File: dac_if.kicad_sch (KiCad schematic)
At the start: 0 parts

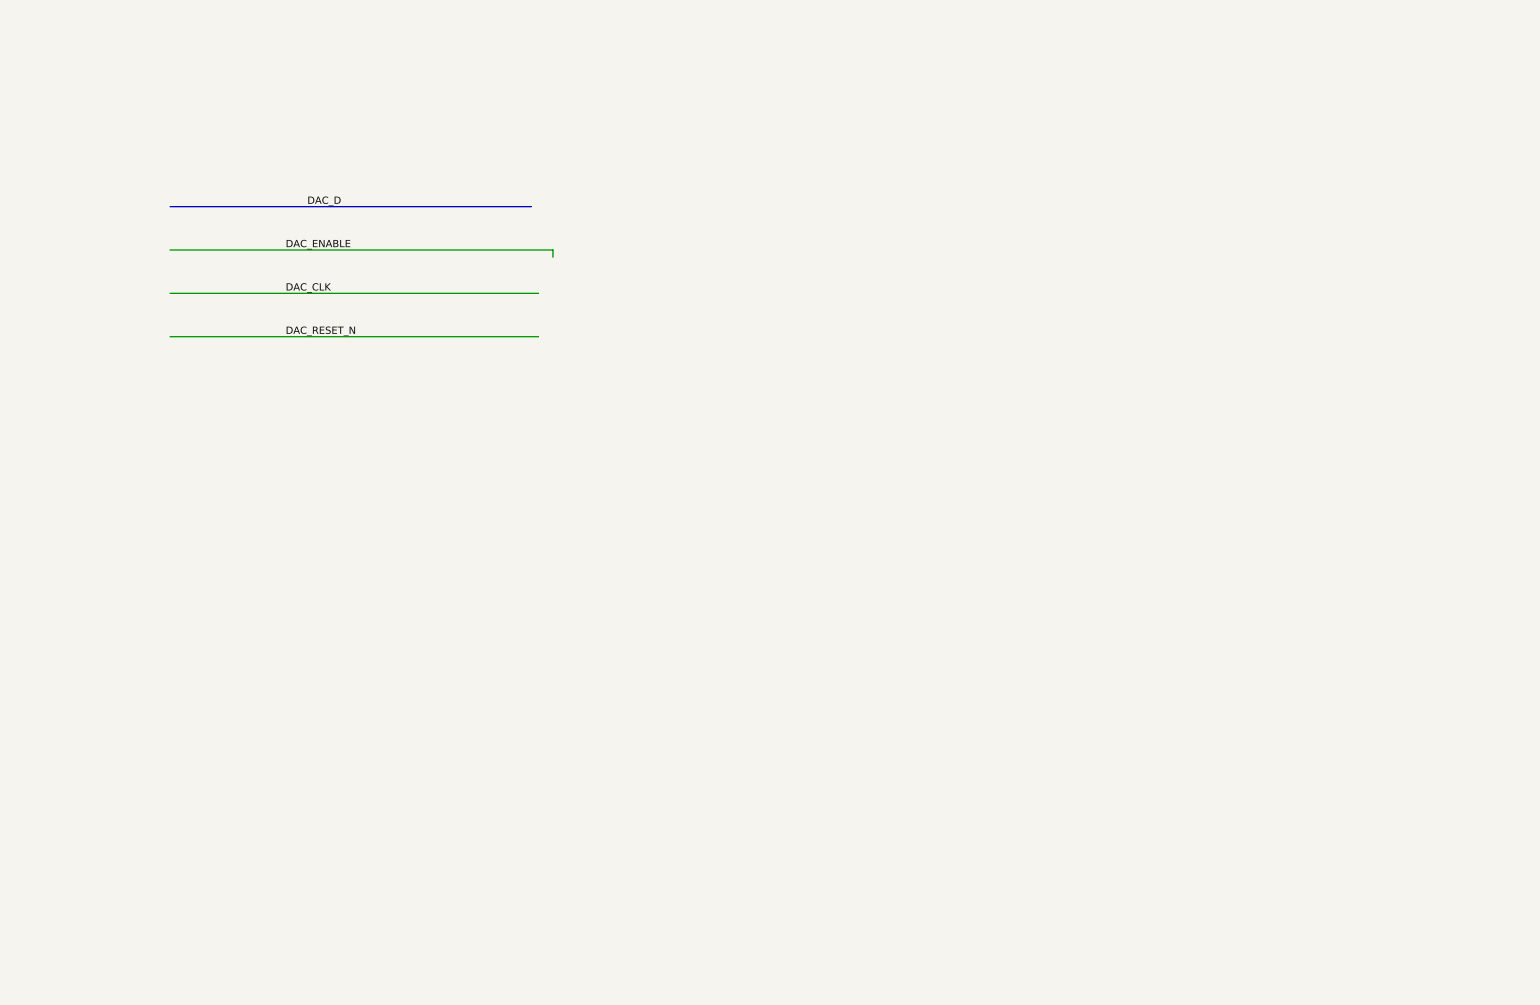
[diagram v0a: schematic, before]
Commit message: Turn to new version Kicad
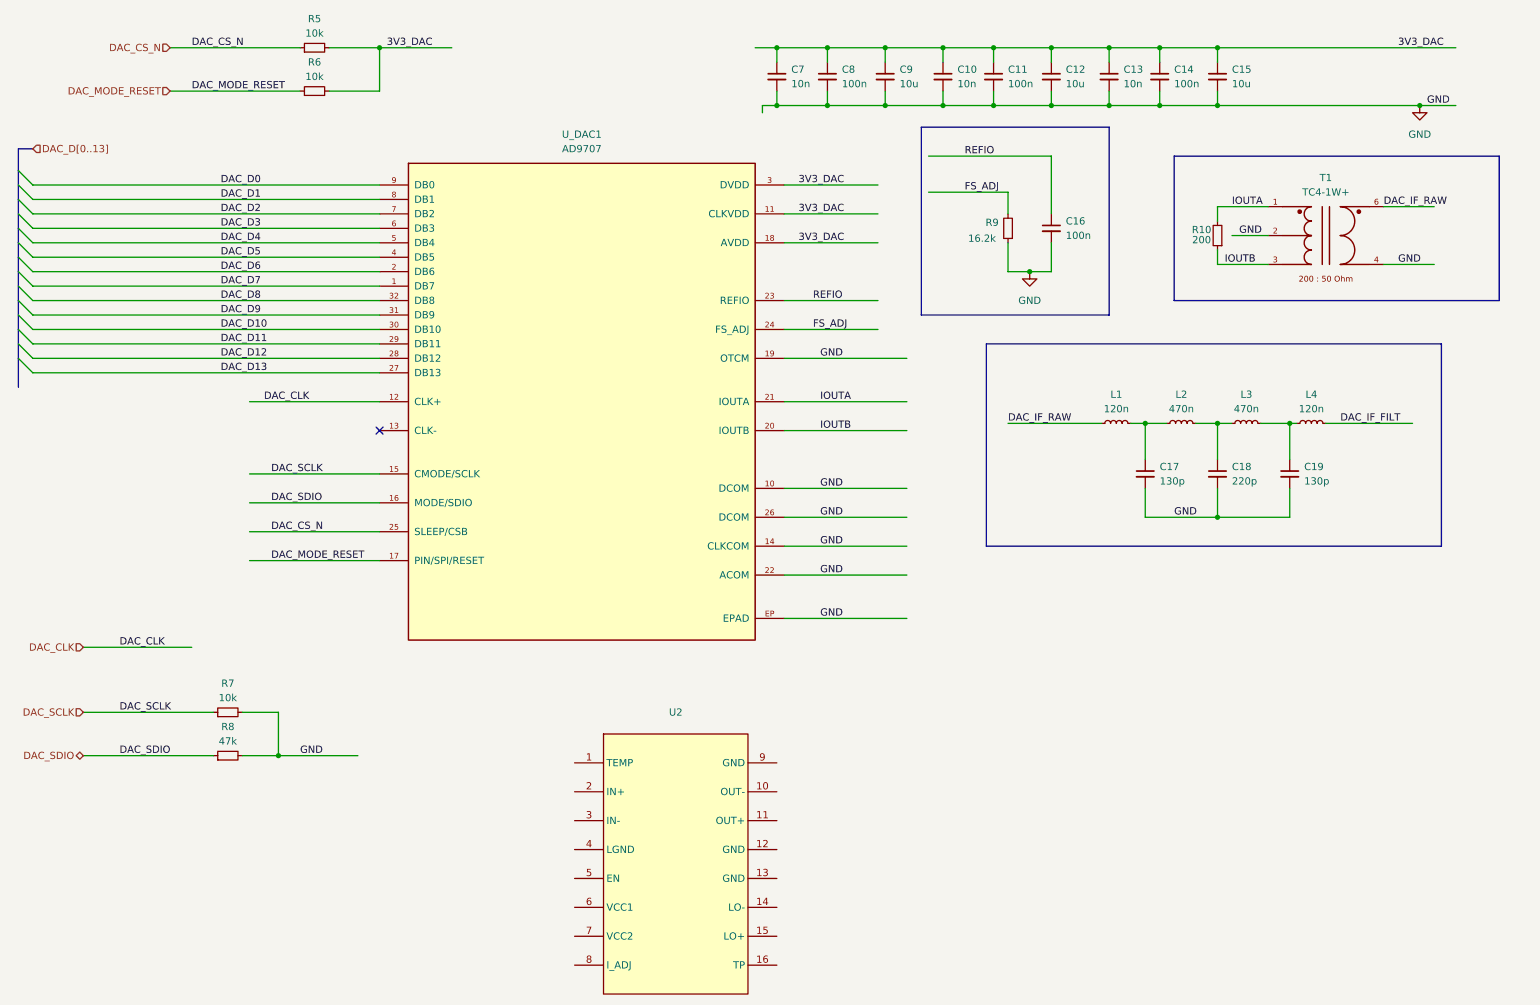
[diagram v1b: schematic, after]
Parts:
- added C10, C13, C7: 10n, Capacitor_SMD:C_0603_1608Metric, symbol Device:C_Small
- added C11, C14, C8: 100n, Capacitor_SMD:C_0603_1608Metric, symbol Device:C_Small
- added C12, C15, C9: 10u, Capacitor_SMD:C_1206_3216Metric, symbol Device:C_Small
- added C16: 100n, Capacitor_SMD:C_1206_3216Metric, symbol Device:C_Small
- added C17, C19: 130p, Capacitor_SMD:C_0603_1608Metric, symbol Device:C_Small
- added C18: 220p, Capacitor_SMD:C_0603_1608Metric, symbol Device:C_Small
- added L1, L4: 120n, Inductor_SMD:L_0603_1608Metric_Pad1.05x0.95mm_HandSolder, symbol Device:L_Small
- added L2, L3: 470n, Inductor_SMD:L_0603_1608Metric_Pad1.05x0.95mm_HandSolder, symbol Device:L_Small
- added R10: 200, Resistor_SMD:R_0603_1608Metric_Pad0.98x0.95mm_HandSolder, symbol Device:R_Small
- added R5, R6, R7: 10k, Resistor_SMD:R_0603_1608Metric_Pad0.98x0.95mm_HandSolder, symbol Device:R_Small
- added R8: 47k, Resistor_SMD:R_0603_1608Metric_Pad0.98x0.95mm_HandSolder, symbol Device:R_Small
- added R9: 16.2k, Resistor_SMD:R_0603_1608Metric_Pad0.98x0.95mm_HandSolder, symbol Device:R_Small
- added T1: TC4-1W+, GNSS_Transformers:TC4-1W_AT224-1A, symbol GNSS_Transformers:TC4-1W+
- added U2: (no value), Package_DFN_QFN:QFN-16-1EP_3x3mm_P0.5mm_EP1.7x1.7mm_ThermalVias, symbol gnss-lib:LTC5510
- added U_DAC1: AD9707, Package_CSP:LFCSP-32-1EP_5x5mm_P0.5mm_EP3.1x3.1mm, symbol GNSS_Draft:AD9707_RevF
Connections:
- net DAC_CLK: now also U_DAC1.12 (CLK+)
- new net: C18.1, L2.2, L3.1
- new net: C19.1, L3.2, L4.1
- new net: C17.1, L1.2, L2.1
- new net 3V3_DAC: C10.1, C11.1, C12.1, C13.1, C14.1, C15.1, C7.1, C8.1, C9.1, R5.2, R6.2, U_DAC1.11 (CLKVDD), U_DAC1.18 (AVDD), U_DAC1.3 (DVDD)
- new net DAC_CS_N: R5.1, U_DAC1.25 (SLEEP/CSB)
- new net DAC_D0: U_DAC1.9 (DB0)
- new net DAC_D1: U_DAC1.8 (DB1)
- new net DAC_D10: U_DAC1.30 (DB10)
- new net DAC_D11: U_DAC1.29 (DB11)
- new net DAC_D12: U_DAC1.28 (DB12)
- new net DAC_D13: U_DAC1.27 (DB13)
- new net DAC_D2: U_DAC1.7 (DB2)
- new net DAC_D3: U_DAC1.6 (DB3)
- new net DAC_D4: U_DAC1.5 (DB4)
- new net DAC_D5: U_DAC1.4 (DB5)
- new net DAC_D6: U_DAC1.2 (DB6)
- new net DAC_D7: U_DAC1.1 (DB7)
- new net DAC_D8: U_DAC1.32 (DB8)
- new net DAC_D9: U_DAC1.31 (DB9)
- new net DAC_IF_FILT: L4.2
- new net DAC_IF_RAW: L1.1, T1.6 (PRI_DOT)
- new net DAC_MODE_RESET: R6.1, U_DAC1.17 (PIN/SPI/RESET)
- new net DAC_SCLK: R7.1, U_DAC1.15 (CMODE/SCLK)
- new net DAC_SDIO: R8.1, U_DAC1.16 (MODE/SDIO)
- new net FS_ADJ: R9.2, U_DAC1.24 (FS_ADJ)
- new net GND: C10.2, C11.2, C12.2, C13.2, C14.2, C15.2, C16.2, C17.2, C18.2, C19.2, C7.2, C8.2, C9.2, R7.2, R8.2, R9.1, T1.2 (SEC_CT), T1.4 (PRI), U_DAC1.10 (DCOM), U_DAC1.14 (CLKCOM), U_DAC1.19 (OTCM), U_DAC1.22 (ACOM), U_DAC1.26 (DCOM), U_DAC1.EP (EPAD)
- new net IOUTA: R10.2, T1.1 (SEC_DOT), U_DAC1.21 (IOUTA)
- new net IOUTB: R10.1, T1.3 (SEC), U_DAC1.20 (IOUTB)
- new net REFIO: C16.1, U_DAC1.23 (REFIO)
- no-connect marks 0 -> 1

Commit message: Make schema of dac and rf partly
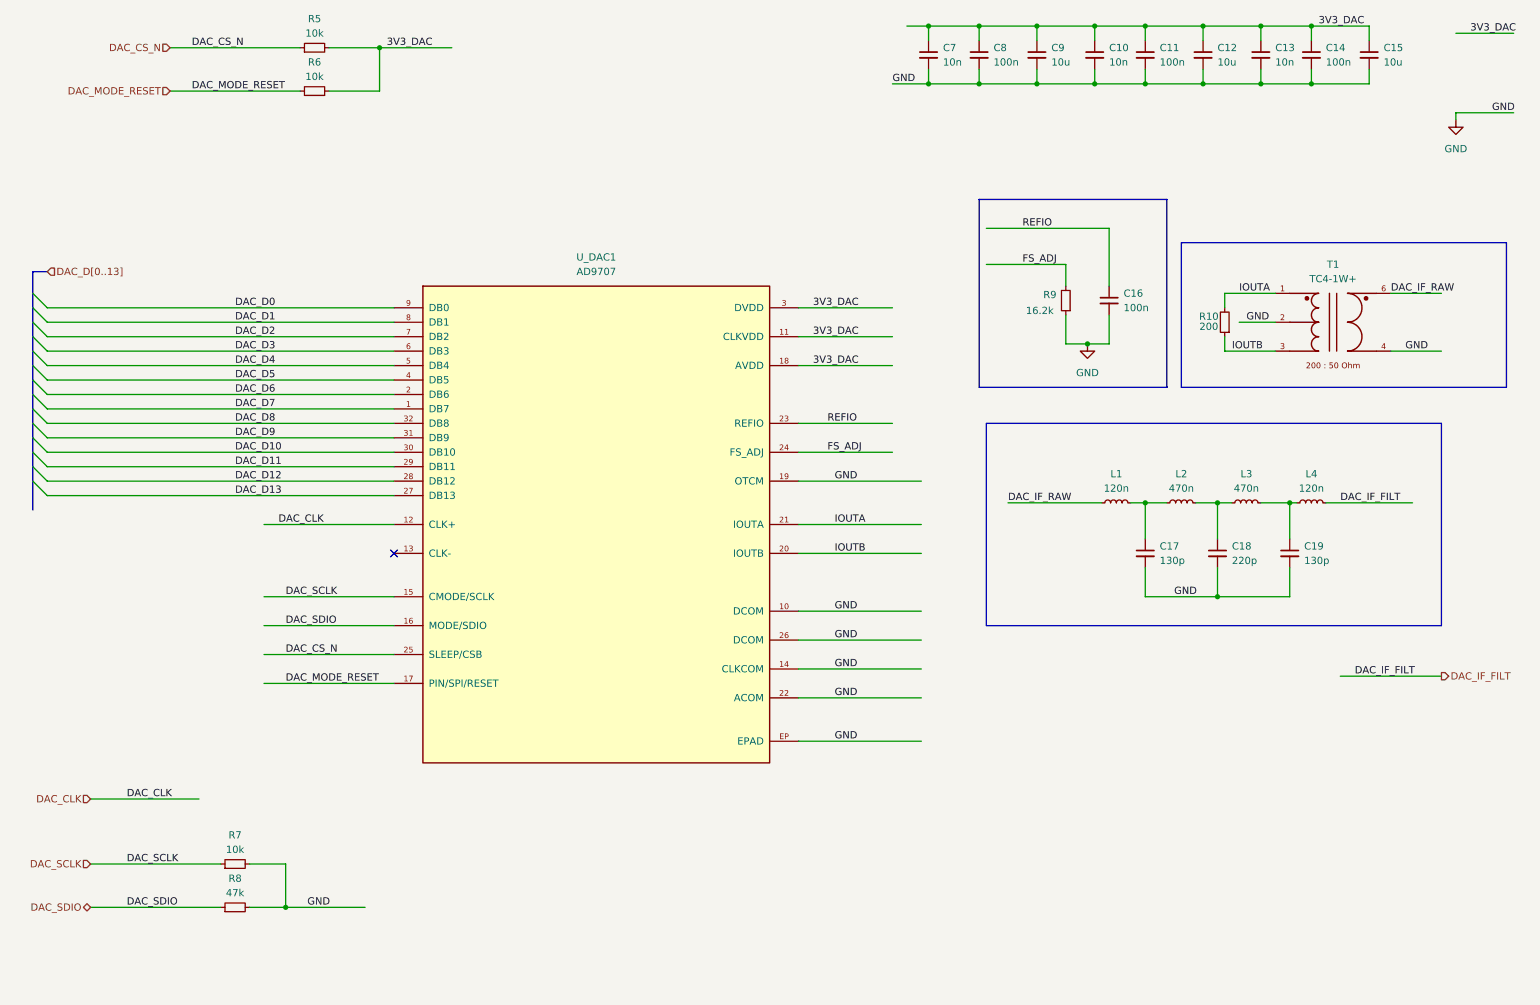
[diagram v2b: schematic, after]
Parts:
- removed U2: (no value), Package_DFN_QFN:QFN-16-1EP_3x3mm_P0.5mm_EP1.7x1.7mm_ThermalVias, symbol gnss-lib:LTC5510
- L1, L4: Производитель Murrata -> Murata
- L2, L3: MPN LQW18ANR12G00D -> LQW18ANR47J00D; Допуск 2% -> 5%; Производитель Murrata -> Murata
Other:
- moved on the sheet: C10, C11, C12, C13, C14, C15, C16, C17, C18, C19, C7, C8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
